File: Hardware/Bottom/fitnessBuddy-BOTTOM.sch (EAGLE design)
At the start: 31 parts, among them U1 AD5242-SO16

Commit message: finished bottom board and schematic
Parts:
- added J1: (no value), LinnesLab-Connectors:CONN_07
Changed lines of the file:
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@@
 <setting verticaltext="up"/>
 </settings>
-<grid distance="1" unitdist="mil" unit="mm" style="lines" multiple="1" display="no" altdistance="5" altunitdist="mil" altunit="mil"/>
+<grid distance="0.1" unitdist="inch" unit="inch" style="lines" multiple="1" display="no" altdistance="0.01" altunitdist="inch" altunit="inch"/>
 <layers>
 <layer number="1" name="Top" color="4" fill="1" visible="no" active="no"/>
@@
 <part name="GND30" library="LinnesLab-Symbols" deviceset="GND" device=""/>
 <part name="SUPPLY24" library="LinnesLab-Symbols" deviceset="3.3V" device=""/>
+<part name="J1" library="LinnesLab-Connectors" deviceset="CONN_07" device=""/>
 </parts>
 <sheets>
@@
 <attribute name="VALUE" x="-17.78" y="30.734" size="1.778" layer="96" align="bottom-center"/>
 </instance>
+<instance part="J1" gate="G$1" x="93.98" y="12.7" smashed="yes">
+<attribute name="VALUE" x="88.9" y="2.794" size="1.778" layer="96" font="vector"/>
+<attribute name="NAME" x="88.9" y="25.908" size="1.778" layer="95" font="vector"/>
+</instance>
 </instances>

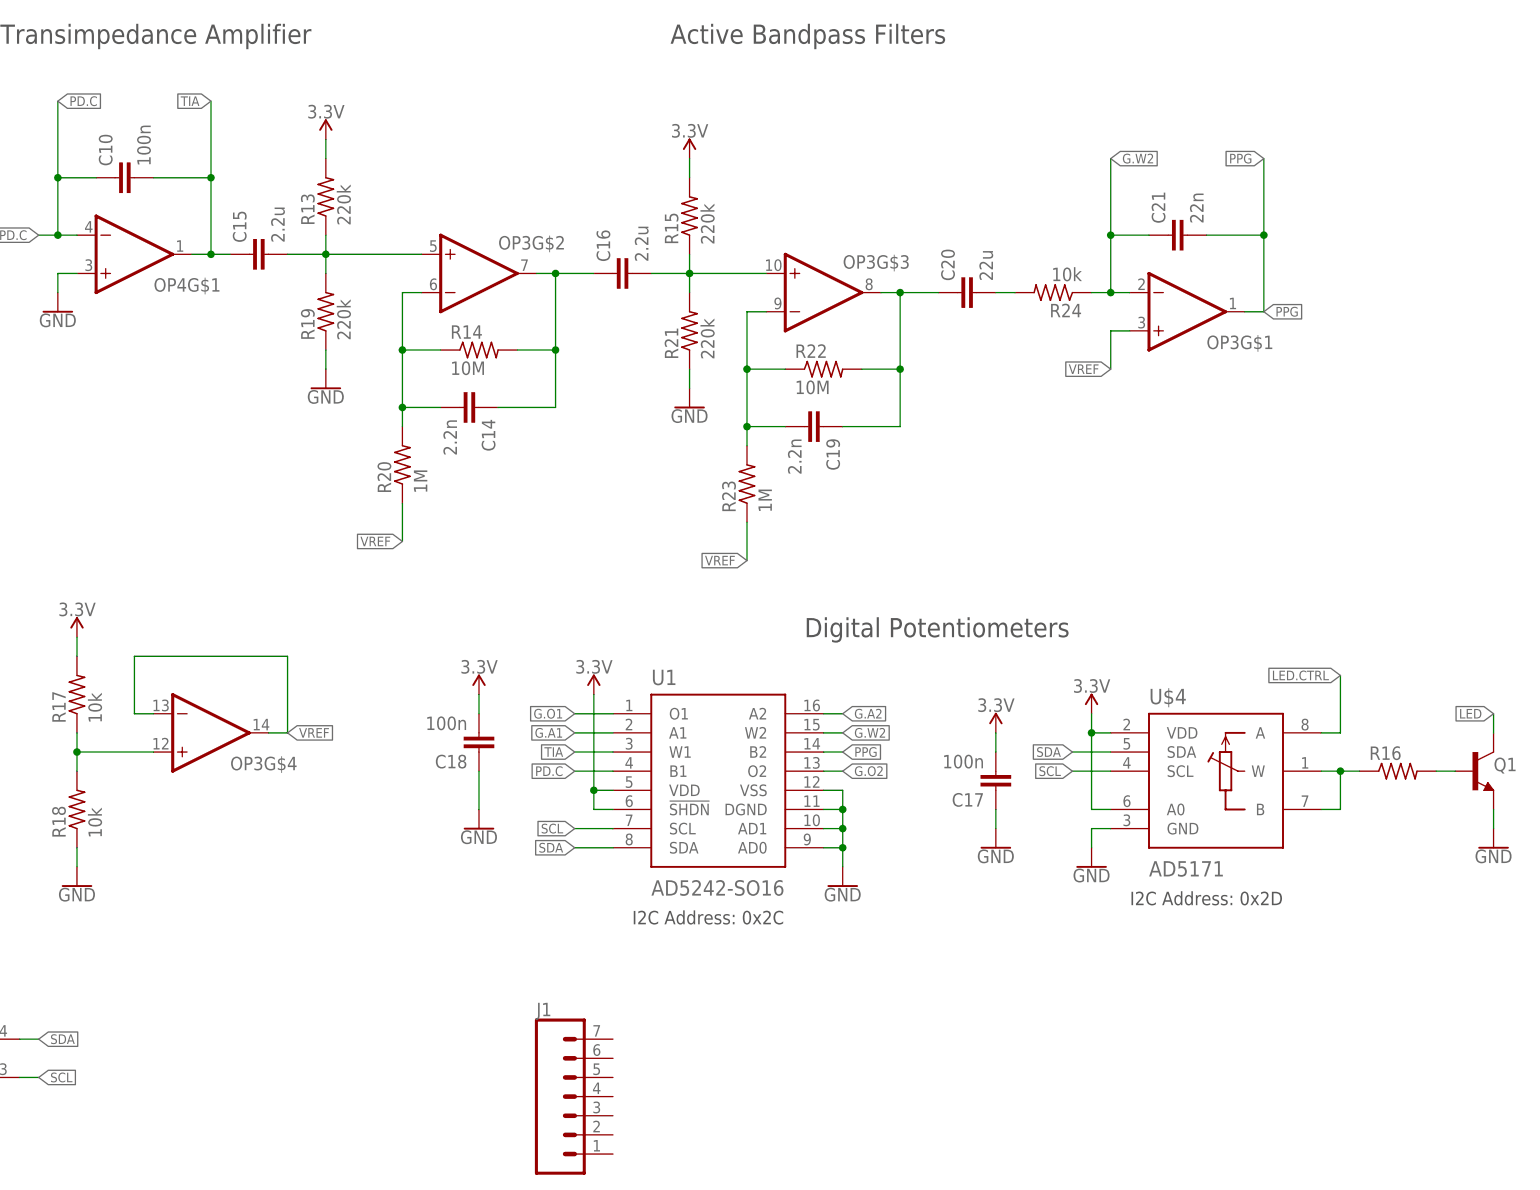
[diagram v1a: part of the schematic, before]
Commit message: started to route bottom board
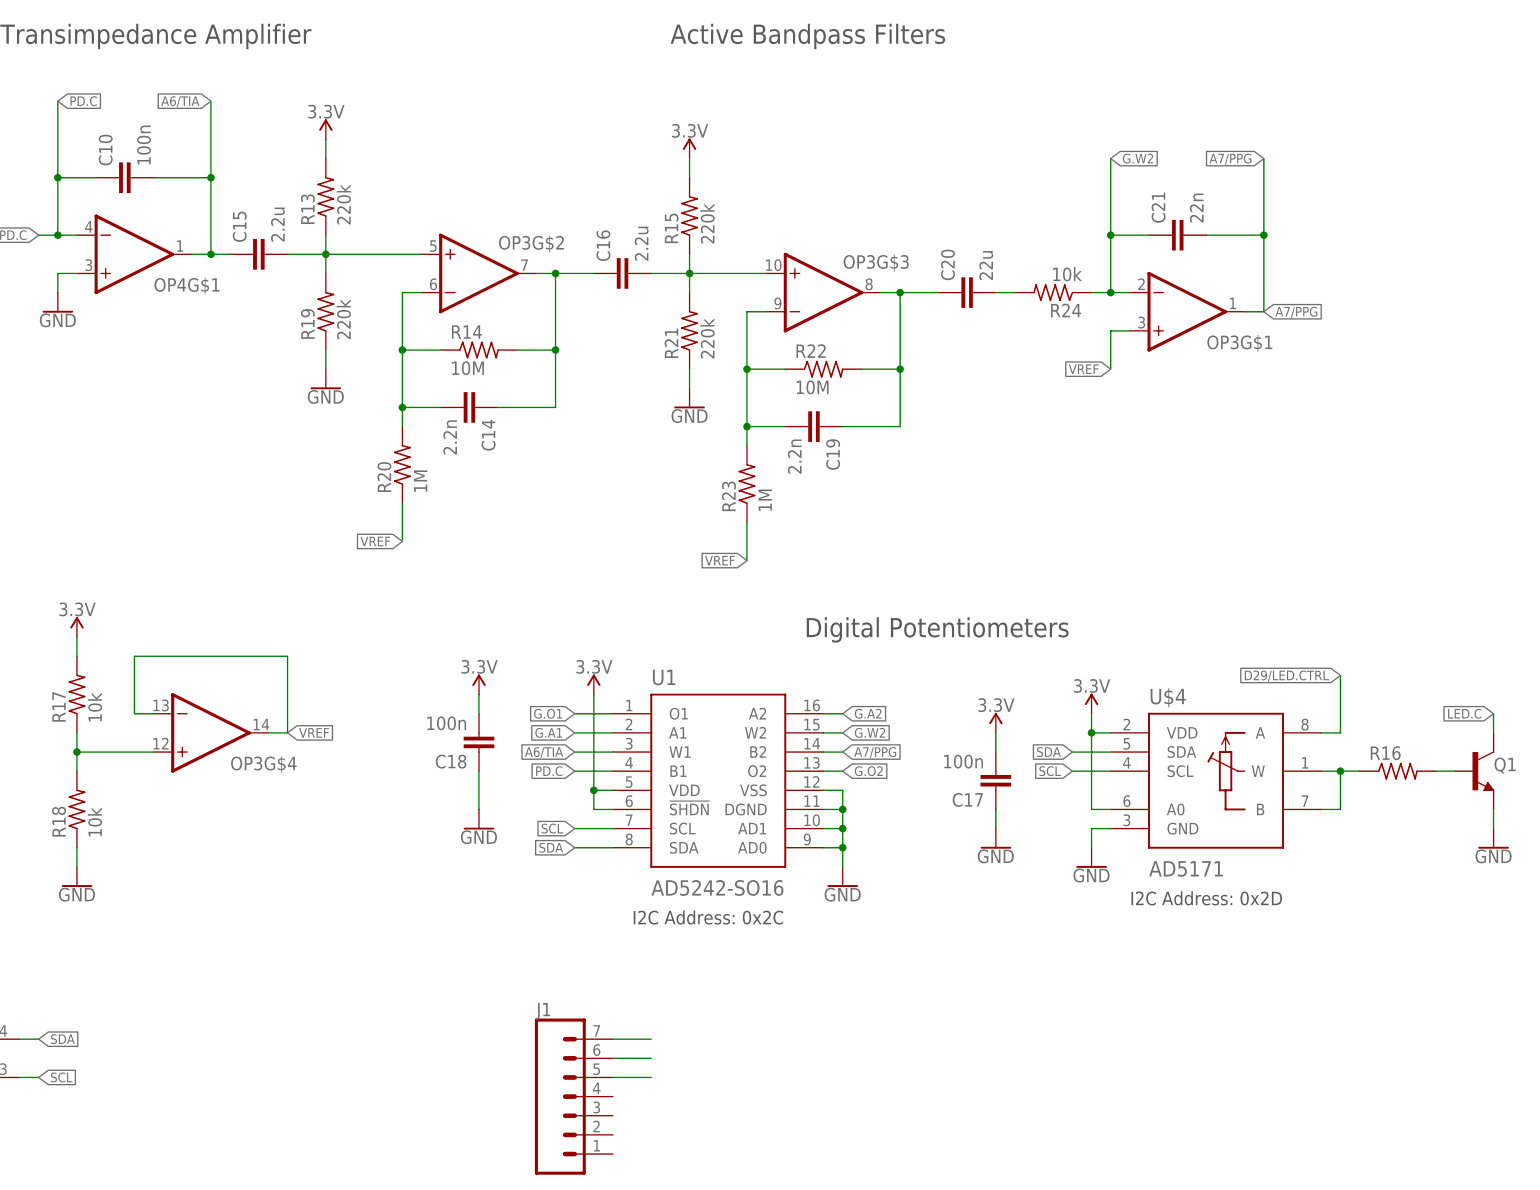
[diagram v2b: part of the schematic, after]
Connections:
- net LED.CTRL renamed D29/LED.CTRL
- net PPG renamed A7/PPG
- net TIA renamed A6/TIA
- removed net LED: Q1.C
- new net N$1: J1.7
- new net N$2: J1.6
- new net N$3: J1.5
- net LED.C: now also Q1.C
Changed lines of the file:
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@@
 </segment>
 </net>
-<net name="TIA" class="0">
+<net name="A6/TIA" class="0">
 <segment>
 <wire x1="99.06" y1="60.96" x2="93.98" y2="60.96" width="0.1524" layer="91"/>
@@
 <label x="0" y="127" size="1.27" layer="95" xref="yes"/>
 </segment>
+<segment>
+<wire x1="215.9" y1="63.5" x2="215.9" y2="66.04" width="0.1524" layer="91"/>
+<label x="215.9" y="66.04" size="1.27" layer="95" rot="R180" xref="yes"/>
+<pinref part="Q1" gate="G$1" pin="C"/>
+</segment>
 </net>
 <net name="VREF" class="0">
@@
 <wire x1="165.1" y1="116.84" x2="165.1" y2="111.76" width="0.1524" layer="91"/>
 <label x="165.1" y="111.76" size="1.27" layer="95" rot="R180" xref="yes"/>
-</segment>
-</net>
-<net name="LED" class="0">
-<segment>
-<wire x1="215.9" y1="63.5" x2="215.9" y2="66.04" width="0.1524" layer="91"/>
-<label x="215.9" y="66.04" size="1.27" layer="95" rot="R180" xref="yes"/>
-<pinref part="Q1" gate="G$1" pin="C"/>
 </segment>
 </net>
@@
 </segment>
 </net>
-<net name="LED.CTRL" class="0">
+<net name="D29/LED.CTRL" class="0">
 <segment>
 <pinref part="U$4" gate="G$1" pin="A"/>
@@
 </segment>
 </net>
-<net name="PPG" class="0">
+<net name="A7/PPG" class="0">
 <segment>
 <wire x1="127" y1="60.96" x2="129.54" y2="60.96" width="0.1524" layer="91"/>
@@
 </segment>
 </net>
+<net name="N$1" class="0">
+<segment>
+<pinref part="J1" gate="G$1" pin="7"/>
+<wire x1="99.06" y1="22.86" x2="104.14" y2="22.86" width="0.1524" layer="91"/>
+</segment>
+</net>
+<net name="N$2" class="0">
+<segment>
+<pinref part="J1" gate="G$1" pin="6"/>
+<wire x1="99.06" y1="20.32" x2="104.14" y2="20.32" width="0.1524" layer="91"/>
+</segment>
+</net>
+<net name="N$3" class="0">
+<segment>
+<pinref part="J1" gate="G$1" pin="5"/>
+<wire x1="99.06" y1="17.78" x2="104.14" y2="17.78" width="0.1524" layer="91"/>
+</segment>
+</net>

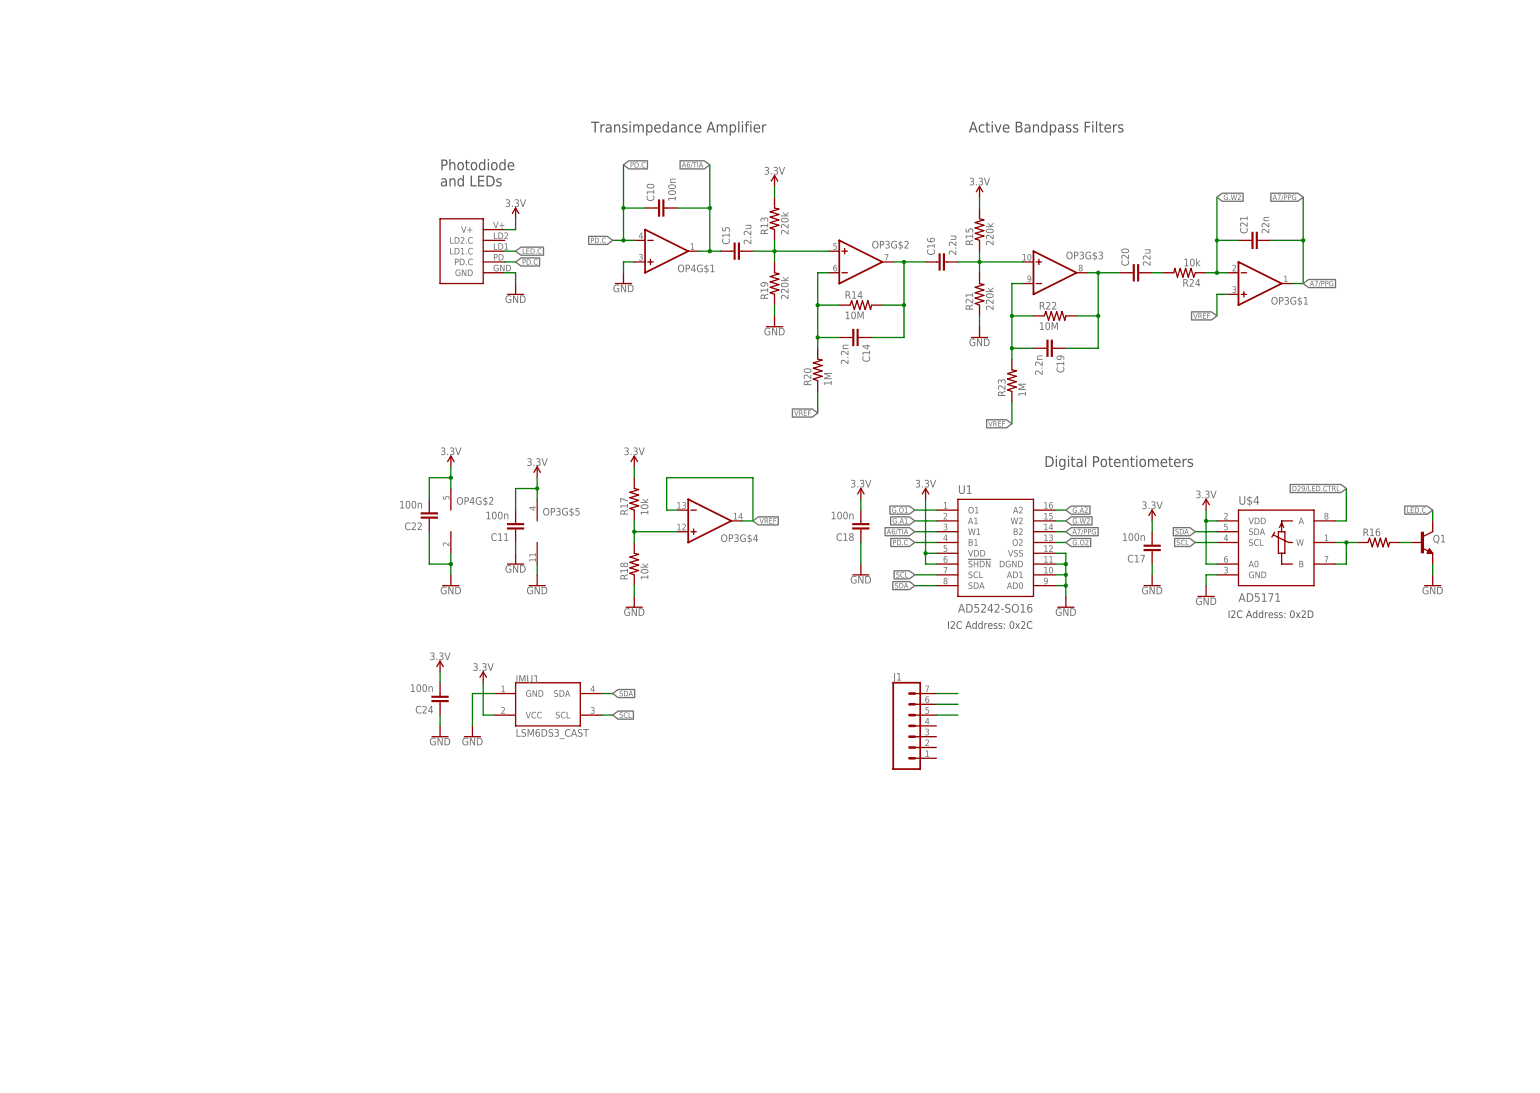
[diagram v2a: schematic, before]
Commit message: Made progress on routing bottom board
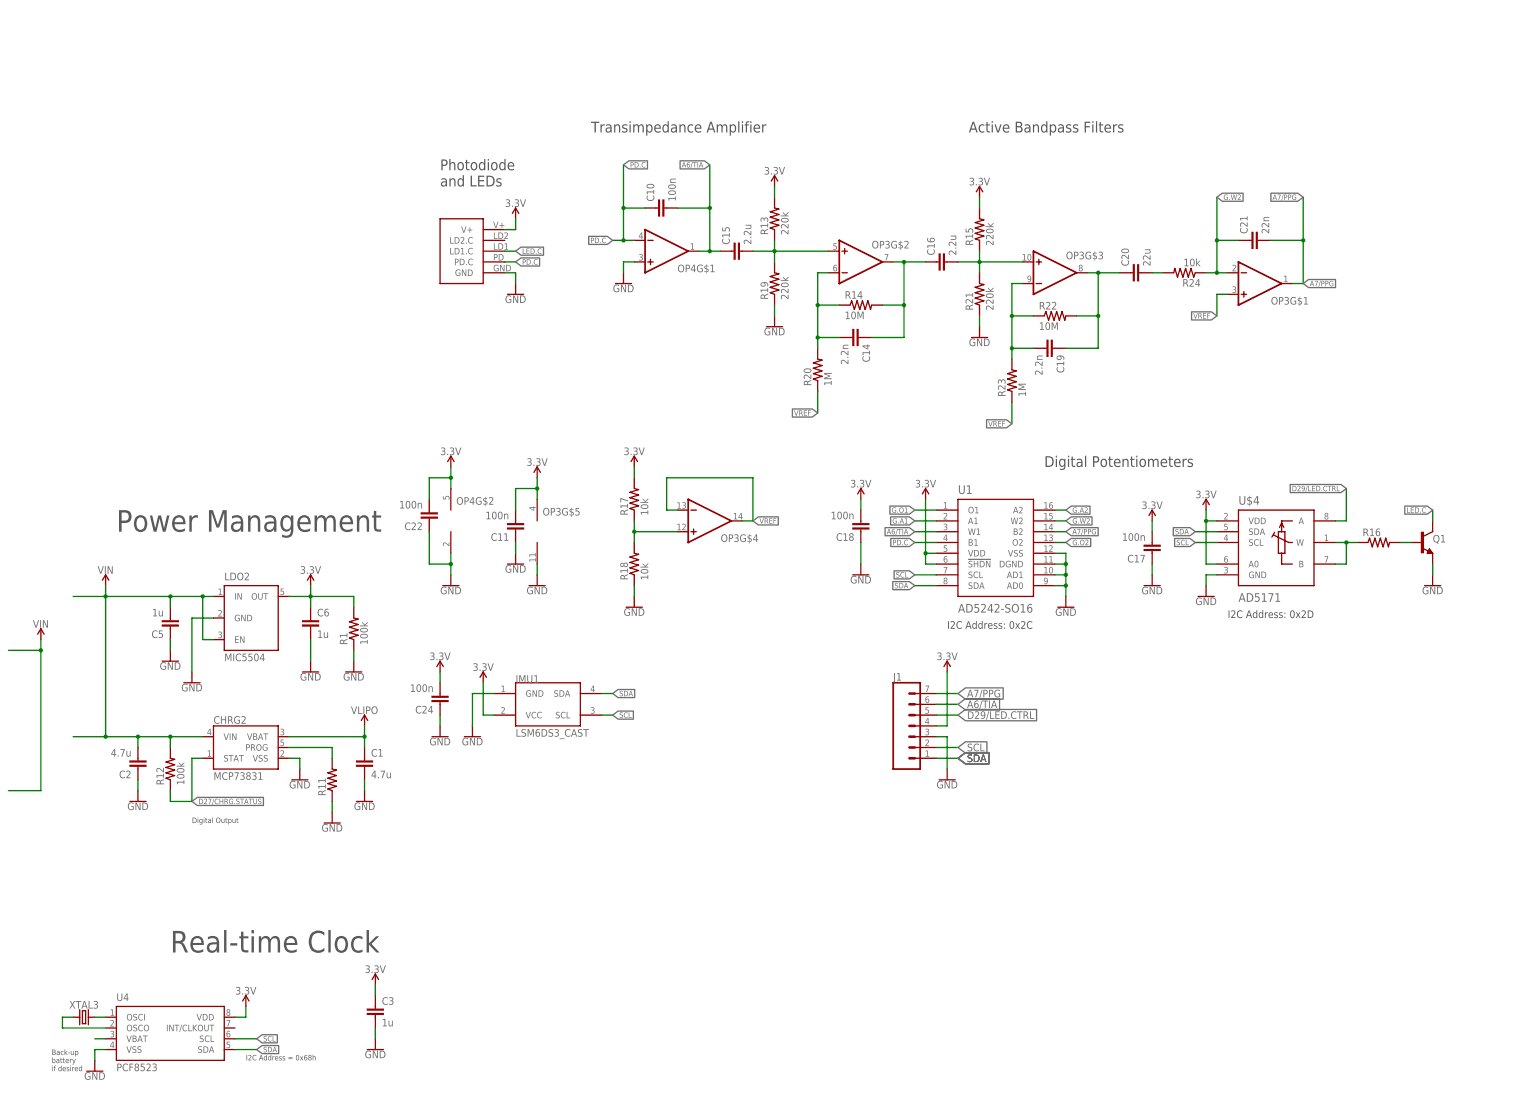
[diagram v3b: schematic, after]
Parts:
- added C1, C2: 4.7u, LinnesLab-Passives:CAPACITOR0603
- added C3, C5, C6: 1u, LinnesLab-Passives:CAPACITOR0603
- added CHRG2: MCP73831, LinnesLab-Power:MCP73831
- added LDO2: MIC5504, LinnesLab-Power:MIC5504
- added R1, R12: 100k, LinnesLab-Passives:RESISTOR0603
- added R11: (no value), LinnesLab-Passives:RESISTOR0603
- added U4: PCF8523, LinnesLab-Clocks:PCF8523
- added XTAL3: 32.7680kHz, LinnesLab-Clocks:CRYSTALECS-.327-12.5-12-C-TR
- J1: device LinnesLab-Connectors:CONN_07 -> LinnesLab-Connectors:CONN_07-1.27MM
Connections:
- removed net N$1: J1.7
- removed net N$2: J1.6
- removed net N$3: J1.5
- new net D27/CHRG.STATUS: CHRG2.STAT, R12.1
- new net N$4: CHRG2.PROG, R11.2
- new net N$5: U4.OSCO, XTAL3.1
- new net N$6: U4.OSCI, XTAL3.2
- new net VBATT: U4.VBAT
- new net VIN: C2.2, C5.2, CHRG2.VIN, LDO2.EN, LDO2.IN, R12.2
- new net VLIPO: C1.1, CHRG2.VBAT
- net 3.3V: now also C3.1, C6.1, J1.4, LDO2.OUT, R1.2, U4.VDD
- net A6/TIA: now also J1.6
- net A7/PPG: now also J1.7
- net D29/LED.CTRL: now also J1.5
- net GND: now also C1.2, C2.1, C3.2, C5.1, C6.2, CHRG2.VSS, J1.3, LDO2.GND, R1.1, R11.1, U4.VSS
- net SCL: now also J1.2, U4.SCL
- net SDA: now also J1.1, U4.SDA
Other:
- note added: "Back-up battery if desired"
- note added: "Digital Output"
- note added: "I2C Address = 0x68h"
- note added: "Power Management"
- note added: "Real-time Clock"

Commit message: finished routing PPG Board
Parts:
- removed U$4: AD5171, LinnesLab-DigitalIC:AD5171
- removed U1: AD5242-SO16, LinnesLab-DigitalIC:AD5242-SO16
- added AD5171: AD5171, LinnesLab-DigitalIC:AD5171
- added AD5242: AD5242-SO16, LinnesLab-DigitalIC:AD5242-SO16
- added C4: 100n, LinnesLab-Passives:CAPACITOR0603
- added LOGO1: REVISION.A, LinnesLab-Logos:REVISION.A
- added LOGO2: OSHW-LOGOS, LinnesLab-Logos:OSHW-LOGOS
- renumbered OP4 to TIA
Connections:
- net 3.3V: now also AD5171.A0, AD5171.VDD, AD5242.!SHDN, AD5242.VDD; no longer U$4.A0, U$4.VDD, U1.!SHDN, U1.VDD
- net A6/TIA: now also AD5242.W1; no longer U1.W1
- net A7/PPG: now also AD5242.B2; no longer U1.B2
- net D29/LED.CTRL: now also AD5171.A; no longer U$4.A
- net G.A1: now also AD5242.A1; no longer U1.A1
- net G.A2: now also AD5242.A2; no longer U1.A2
- net G.O1: now also AD5242.O1; no longer U1.O1
- net G.O2: now also AD5242.O2; no longer U1.O2
- net G.W2: now also AD5242.W2; no longer U1.W2
- net GND: now also AD5171.GND, AD5242.AD0, AD5242.AD1, AD5242.DGND, AD5242.VSS, C4.2; no longer U$4.GND, U1.AD0, U1.AD1, U1.DGND, U1.VSS
- net N$9: now also AD5171.B, AD5171.W; no longer U$4.B, U$4.W
- net PD.C: now also AD5242.B1; no longer U1.B1
- net SCL: now also AD5171.SCL, AD5242.SCL; no longer U$4.SCL, U1.SCL
- net SDA: now also AD5171.SDA, AD5242.SDA; no longer U$4.SDA, U1.SDA
- net VREF: now also C4.1
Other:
- note added: "Castellated IMU breakout"
- note added: "Connection to Optical Sensor Module"
- note added: "Connection to digital potentiometer for dynamic gain control"
- note added: "Connection to upper board"
- note added: "Fitness Buddy PPG Circuit"
- note added: "Vref Generator and Bypass Capacitor"
- moved on the sheet: C11, C17, C18, C22, C24, IMU1, J1, OP3G$4, OP3G$5, Q1, R16, R17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

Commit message: organized top board
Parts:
- removed C1, C2: 4.7u, LinnesLab-Passives:CAPACITOR0603
- removed C5, C6: 1u, LinnesLab-Passives:CAPACITOR0603
- removed CHRG2: MCP73831, LinnesLab-Power:MCP73831
- removed LDO2: MIC5504, LinnesLab-Power:MIC5504
- removed R1, R12: 100k, LinnesLab-Passives:RESISTOR0603
- removed R11: (no value), LinnesLab-Passives:RESISTOR0603
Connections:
- removed net D27/CHRG.STATUS: CHRG2.STAT, R12.1
- removed net N$4: CHRG2.PROG, R11.2
- removed net VIN: C2.2, C5.2, CHRG2.VIN, LDO2.EN, LDO2.IN, R12.2
- removed net VLIPO: C1.1, CHRG2.VBAT
- net 3.3V: no longer C6.1, LDO2.OUT, R1.2
- net GND: no longer C1.2, C2.1, C5.1, C6.2, CHRG2.VSS, LDO2.GND, R1.1, R11.1
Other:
- note removed: "Digital Output"
- note removed: "Power Management"
